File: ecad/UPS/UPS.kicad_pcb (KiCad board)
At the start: 4 copper layers, 121.9 x 139.7 mm, 163 parts, among them J2 Conn_01x02_Pin, J3 USB_C_Receptacle_USB2.0_16P, J4 PROG, J5 Conn_01x02_Pin, J6 Conn_01x02_Pin, J7 Fan_Connector, J8 PJ-002AH, Q1 CSD18540Q5B, Q2 Q_PMOS_DGS, Q3 IRLR7843TRPBF, Q4 Q_PMOS_DGS, Q5 CSD18540Q5B, Q6 CSD18540Q5B, Q7 CSD18540Q5B, Q8 2N7002, SW3 SW_DPDT_x2, U1 BQ25730RSNR, U2 MPQ5031GRE-0001-AEC1-P, U4 STM32L152RCT6, U5 AP2112K-3.3TRG1, U6 BOOT0, U7 NRST

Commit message: MCU routing
Routed most of MCU
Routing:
- net /Charger/bat_th1: track 0.00 -> 234.9 mm, vias 0 -> 4
- net /Charger/cmp_out: track 0.00 -> 216.1 mm, vias 0 -> 6
- net /Charger/PROCHOT_N: track 0.00 -> 146.7 mm, vias 0 -> 4
- net +3.3V: track 0.00 -> 136.6 mm, vias 0 -> 2
- net GND: track 27.8 -> 151.2 mm, vias 19 -> 21
- net /Charger/bat_th3: track 0.00 -> 120.5 mm, vias 0 -> 5
- net /Charger/bat_th2: track 0.00 -> 119.4 mm, vias 0 -> 4
- net /Output/vsel2: track 0.00 -> 89.6 mm, vias 0 -> 4
- net /controller/PB0: track 0.00 -> 82.5 mm, vias 0 -> 2
- net 3.3V: track 0.00 -> 80.3 mm, vias 0 -> 4
- net /Output/SDA: track 0.00 -> 80.1 mm, vias 0 -> 2
- net Net-(U4B-BOOT0): track 0.00 -> 76.6 mm, vias 0 -> 2
- net /Output/vsel1: track 0.00 -> 71.1 mm, vias 0 -> 2
- net /Output/SCL: track 0.00 -> 70.8 mm
- net NRST: track 0.00 -> 56.5 mm, vias 0 -> 4
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
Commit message: late night grind
Add battery and board thermistor circuits on PC0/PC1.

Implement ADC sampling, temperature conversion, and sensor fault reporting.

Enable the STM32 ADC drivers and poll temperatures in the main loop.

Add the OLED connector on PB10/PB11 and update PCB footprints and net assignments.

Add a Raspberry Pi mounting-hole footprint.

Exclude local docs and test folders from Git.
- checked routing
- messed with firmware
- planning final touches
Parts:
- added ?: , , F.Cu at (154.5, 159.5)
- added C71: 100nF, Capacitor_SMD:C_0805_2012Metric, F.Cu at (29.4, 135.5)
- added C72: 100nF, Capacitor_SMD:C_0805_2012Metric, F.Cu at (29.4, 138.5)
- added J10: NTC_10K_B3950, Connector_PinHeader_2.54mm:PinHeader_1x04_P2.54mm_Vertical, F.Cu at (19.0, 149.7)
- added J9: OLED_3V3_I2C2, Connector_PinHeader_2.54mm:PinHeader_1x04_P2.54mm_Vertical, F.Cu at (10.0, 136.2)
- added R45: 10k 1%, Resistor_SMD:R_0805_2012Metric, F.Cu at (29.4, 141.5)
- added R46: 10k 1%, Resistor_SMD:R_0805_2012Metric, F.Cu at (29.4, 144.4)
- added REF**: pi5_MountingHole_2.2mm_M2_Pad_58mm*49mm, UPS:MountingHole_2.2mm_M2_Pad_58mm_49mm_pi5, F.Cu at (197.5, 161.5)
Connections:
- U4 pad 29: unconnected-(U4B-PB10-Pad29) -> /controller/OLED_SCL
- U4 pad 30: unconnected-(U4B-PB11-Pad30) -> /controller/OLED_SDA
- U4 pad 8: unconnected-(U4B-PC0-Pad8) -> /controller/TEMP_BAT
- U4 pad 9: unconnected-(U4B-PC1-Pad9) -> /controller/TEMP_BOARD

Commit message: Organize UPS placement for Pi 5 mounting and power-stage review
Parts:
- removed ?: , 
- removed C65: 1nF, Capacitor_SMD:C_0603_1608Metric_Pad1.08x0.95mm_HandSolder
- removed C71: 100nF, Capacitor_SMD:C_0805_2012Metric
- removed R42: 4.7k, Resistor_SMD:R_0805_2012Metric
- removed R45: 10k 1%, Resistor_SMD:R_0805_2012Metric
- removed REF**: pi5_MountingHole_2.2mm_M2_Pad_58mm*49mm, UPS:MountingHole_2.2mm_M2_Pad_58mm_49mm_pi5
- added C73: 100 nF, Capacitor_SMD:C_0603_1608Metric, F.Cu at (107.0, 125.0)
- added H1: Pi5_M2.5_NPTH, MountingHole:MountingHole_2.7mm_M2.5, F.Cu at (83.5, 103.0)
- added H2: Pi5_M2.5_NPTH, MountingHole:MountingHole_2.7mm_M2.5, F.Cu at (141.5, 103.0)
- added H3: Pi5_M2.5_NPTH, MountingHole:MountingHole_2.7mm_M2.5, F.Cu at (83.5, 152.0)
- added H4: Pi5_M2.5_NPTH, MountingHole:MountingHole_2.7mm_M2.5, F.Cu at (141.5, 152.0)
- added J11: BAT3_10K_NTC, Connector_JST:JST_XH_B2B-XH-A_1x02_P2.50mm_Vertical, F.Cu at (54.3, 113.0)
- added J12: PI_UART, Connector_PinHeader_2.54mm:PinHeader_1x03_P2.54mm_Vertical, F.Cu at (53.0, 166.0)
- added R47: 10k 1%, Resistor_SMD:R_0805_2012Metric_Pad1.20x1.40mm_HandSolder, F.Cu at (103.5, 125.0)
- C39, C40, C41, C42, C43, C44: footprint Capacitor_SMD:C_0603_1608Metric -> Capacitor_SMD:C_1210_3225Metric
- C51, C52, C53, C54, C55, C56, C57: footprint Capacitor_SMD:C_0603_1608Metric -> Capacitor_SMD:C_0805_2012Metric
- J10: value NTC_10K_B3950 -> BOARD_10K_NTC
- J2: value Conn_01x02_Pin -> BAT1_10K_NTC
- J5: value Conn_01x02_Pin -> BAT2_10K_NTC
- J6: value Conn_01x02_Pin -> BAT4_10K_NTC
- R24, R28, R34: value 68.1k -> 10k 1%
- U1: footprint UPS:RSN0032B-IPC_C -> Package_DFN_QFN:Texas_RSN_WQFN-32-1EP_4x4mm_P0.4mm_EP2.8x2.8mm
- moved J2 95.4 mm to (54.3, 90.0), turned to 90 degrees
- moved U2 93.5 mm to (145.0, 48.0)
- moved COUT1 88.4 mm to (98.0, 121.0), turned to 90 degrees
- moved L2 86.1 mm to (154.0, 71.5), turned to -90 degrees
- moved R40 83.5 mm to (139.0, 41.0)
- moved J6 83.5 mm to (54.3, 74.5), turned to 90 degrees
- moved SW3 80.8 mm to (89.0, 85.0)
- moved CIN1 73.1 mm to (90.0, 121.0), turned to 90 degrees
- moved C20 72.5 mm to (152.0, 84.5)
- moved C64 70.5 mm to (140.5, 56.0)
- moved C9 69.6 mm to (141.0, 46.0), turned to 90 degrees
- moved J5 68.7 mm to (54.3, 102.0), turned to 90 degrees
- moved PS1 67.4 mm to (154.0, 87.5), turned to 0 degrees
- moved R7 67.2 mm to (149.5, 41.0), turned to 90 degrees
- moved J3 67.0 mm to (167.5, 47.5)
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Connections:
- net /Charger/bat_th3 renamed /Charger/bat_th4
- J10 pad 2: /controller/TEMP_BAT -> unconnected-(J10-Pin_2-Pad2)
- U4 pad 20: Net-(U4B-PA4) -> unconnected-(U4B-PA4-Pad20)
- U4 pad 58: unconnected-(U4B-PB6-Pad58) -> /controller/PI_UART_TX
- U4 pad 59: unconnected-(U4B-PB7-Pad59) -> /controller/PI_UART_RX
- U4 pad 8: /controller/TEMP_BAT -> bat_th3
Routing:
- net /Charger/bat_th1: track 234.9 -> 2.43 mm, vias 4 -> 1
- net /Charger/cmp_out: track 216.1 -> 13.3 mm, vias 6 -> 2
- net /Charger/PROCHOT_N: track 146.7 -> 22.8 mm, vias 4 -> 2
- net /Charger/bat_th4: track 120.5 -> 0.00 mm, vias 5 -> 0
- net /Charger/bat_th2: track 119.4 -> 20.9 mm, vias 4 -> 1
- net GND: track 151.2 -> 61.1 mm, vias 21 -> 8
- net /Output/SDA: track 80.1 -> 12.7 mm
- net /controller/PB0: track 82.5 -> 16.9 mm
- net Net-(U4B-BOOT0): track 76.6 -> 13.4 mm, vias 2 -> 0
- net /Output/SCL: track 70.8 -> 12.8 mm
- net Net-(U2-VDD): track 53.8 -> 0.00 mm
- net /Output/vsel1: track 71.1 -> 23.5 mm, vias 2 -> 1
- net Net-(D8-A): track 49.0 -> 3.44 mm
- net 3.3V: track 80.3 -> 37.2 mm, vias 4 -> 2
- net Net-(U1-LODRV1): track 34.0 -> 0.00 mm
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- added copper zone on B.Cu, net GND
- added copper zone on F.Cu, net GND
- removed copper zone on F.Cu, net /Charger/Charger_VBUS_IN
- removed copper zone on F.Cu, net Net-(U1-SW2)
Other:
- board text added: "5V POUR"
- board text added: "BATTERY + BUS CORRIDOR / SIZE FROM TEAM CALCS"
- board text added: "INPUT -> CHARGER -> VSYS -> BOOST -> OUTPUT"
- board text added: "PI 5 ENVELOPE / UPS BELOW / CHECK STANDOFF HEIGHT"
- board text added: "PLACEMENT CANDIDATE - NOT ROUTED / NOT FOR FAB"
- board text added: "QUIET CONTROL / KEEP SWITCH RETURNS LOCAL"
- board text added: "VBUS POUR"
- board text added: "VSYS POUR"

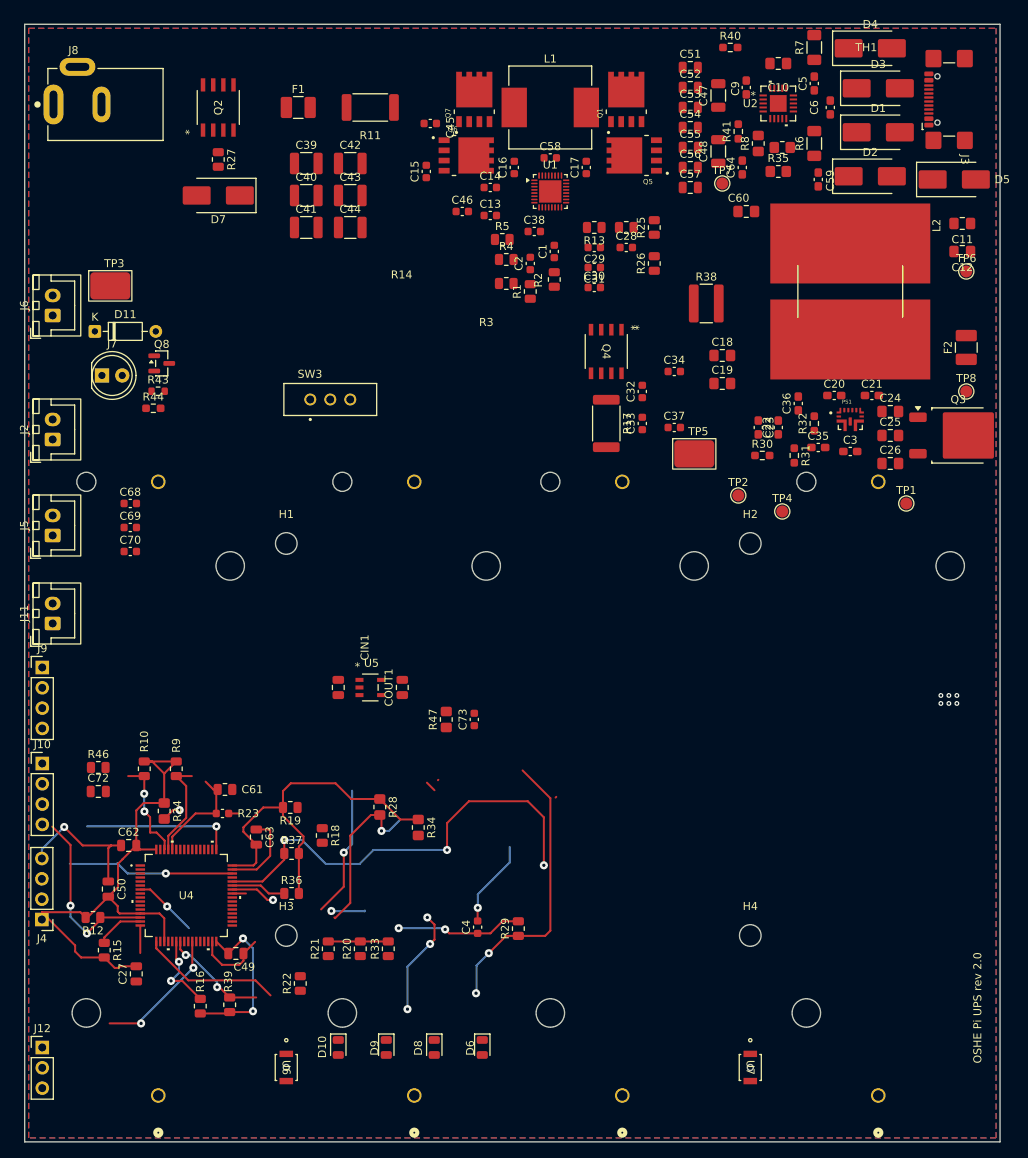
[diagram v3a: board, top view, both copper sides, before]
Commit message: Trial-route boost stage and define local power copper
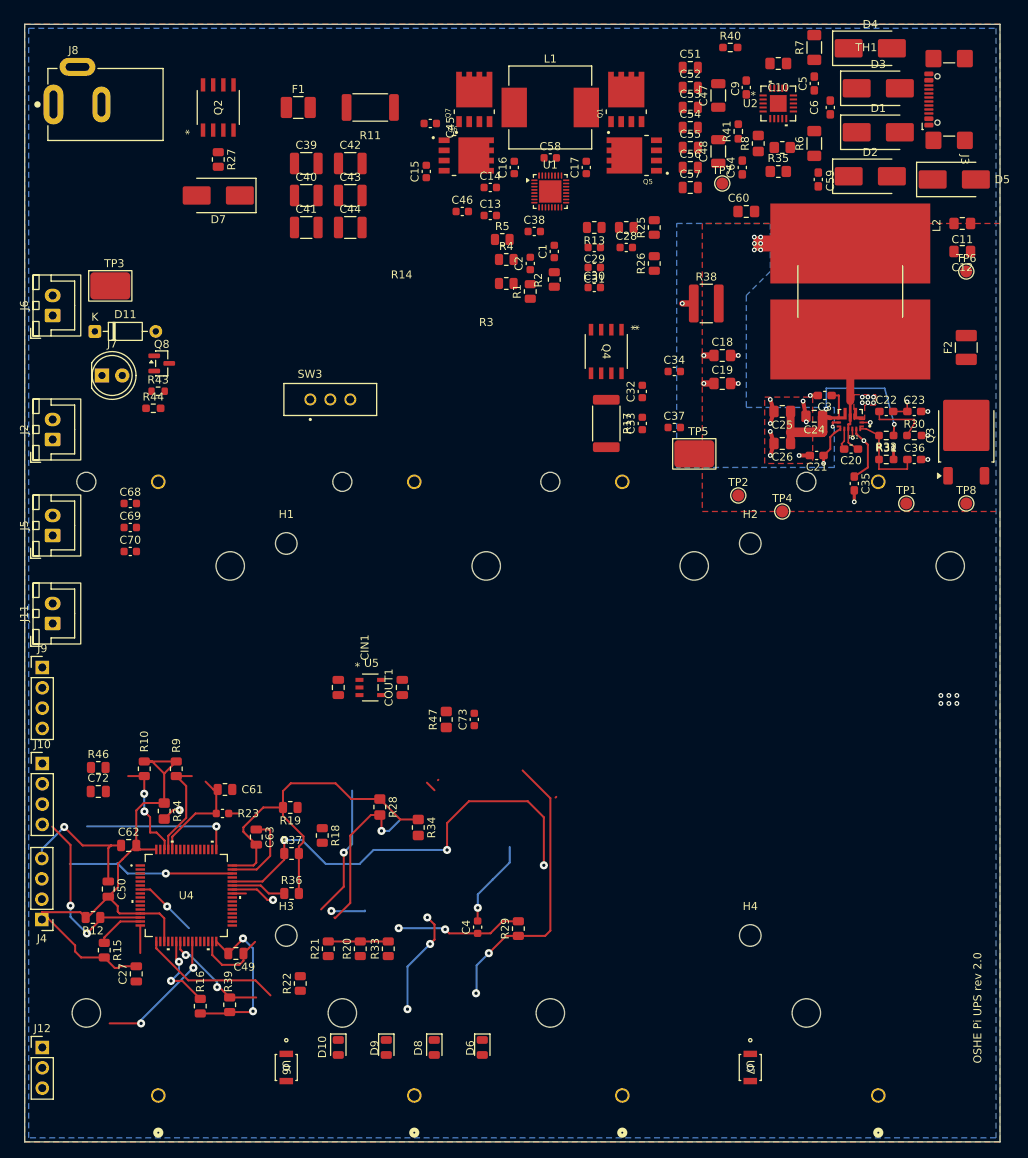
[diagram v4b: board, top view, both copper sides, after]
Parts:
- moved C23 19.6 mm to (162.0, 86.5), turned to 0 degrees
- moved R30 19.2 mm to (162.0, 89.5)
- moved C36 16.1 mm to (162.0, 92.5), turned to 0 degrees
- moved TP8 14.0 mm to (168.5, 98.0)
- moved C25 13.8 mm to (145.5, 86.5), turned to 180 degrees
- moved C26 13.7 mm to (145.5, 90.5), turned to 180 degrees
- moved C22 13.6 mm to (158.5, 86.5), turned to 0 degrees
- moved R31 11.5 mm to (158.5, 92.5), turned to 0 degrees
- moved C21 10.2 mm to (149.8, 92.0), turned to 180 degrees
- moved C24 9.52 mm to (149.5, 87.1), turned to 180 degrees
- moved R32 9.12 mm to (158.5, 89.5), turned to 180 degrees
- moved C3 7.70 mm to (150.8, 84.5), turned to 180 degrees
- moved C20 7.02 mm to (154.1, 91.2), turned to 180 degrees
- moved C35 6.36 mm to (154.5, 95.5), turned to -90 degrees
- moved Q3 1.00 mm to (168.5, 89.5), turned to 90 degrees
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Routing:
- net /BoostConvertor/vbus: track 0.00 -> 32.7 mm, vias 0 -> 2
- net GND: track 61.1 -> 80.7 mm, vias 8 -> 30
- net /BoostConvertor/Vcc: track 0.00 -> 15.4 mm, vias 0 -> 2
- net Net-(PS1-FB): track 0.00 -> 11.5 mm
- net Net-(PS1-VIN): track 0.00 -> 11.5 mm, vias 0 -> 10
- net Net-(C20-Pad1): track 0.00 -> 10.1 mm
- net Net-(PS1-COMP): track 0.00 -> 9.58 mm, vias 0 -> 2
- net Net-(C22-Pad1): track 0.00 -> 7.62 mm
- net Net-(PS1-BST): track 0.00 -> 2.75 mm
- added copper zone on B.Cu, net Net-(PS1-VIN)

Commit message: meow
basicaly nothing
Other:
- board text removed: "PI 5 ENVELOPE / UPS BELOW / CHECK STANDOFF HEIGHT"
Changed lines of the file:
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@@
+	)
+	(gr_line
+		(start 150 99)
+		(end 145.5 99)
+		(stroke
+			(width 0.2)
+			(type default)
+		)
+		(layer "F.Cu")
+		(net "/BoostConvertor/Vcc")
+	)
+	(gr_line
+		(start 154.5 94.5)
+		(end 150 99)
+		(stroke
+			(width 0.2)
+			(type default)
+		)
+		(layer "F.Cu")
+		(net "/BoostConvertor/Vcc")
 	)
 	(gr_line
@@
 	(gr_text "PLACEMENT CANDIDATE - NOT ROUTED / NOT FOR FAB"
 		(at 111 175.5 0)
-		(layer "Dwgs.User")
-		(effects
-			(font
-				(size 0.85 0.85)
-				(thickness 0.15)
-			)
-		)
-	)
-	(gr_text "PI 5 ENVELOPE / UPS BELOW / CHECK STANDOFF HEIGHT"
-		(at 118 114 0)
 		(layer "Dwgs.User")
 		(effects
@@
 			)
 		)
-	)
-	(zone
-		(net "GND")
-		(layer "F.Cu")
-		(name "GND_F.Cu")
-		(hatch edge 0.5)
-		(connect_pads
-			(clearance 0.25)
-		)
-		(min_thickness 0.2)
-		(fill yes
-			(thermal_gap 0.25)
-			(thermal_bridge_width 0.4)
-			(island_removal_mode 0)
-		)
-		(polygon
-			(pts
-				(xy 50.8 38.1) (xy 172.72 38.1) (xy 172.72 63) (xy 135.5 63) (xy 135.5 99) (xy 172.72 99) (xy 172.72 177.8)
-				(xy 50.8 177.8)
-			)
-		)

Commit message: bazinga
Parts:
- J11, J2, J5, J6: moved to B.Cu
- moved J5 92.9 mm to (141.5, 134.0)
- moved J2 92.2 mm to (141.5, 120.0)
- moved C68 80.2 mm to (131.0, 142.0)
- moved C69 73.5 mm to (125.0, 142.0)
- moved C70 66.9 mm to (119.0, 142.0)
- moved J6 66.3 mm to (83.5, 134.0)
- moved R24 50.8 mm to (119.0, 139.0), turned to 0 degrees
- moved U6 48.5 mm to (132.0, 167.0)
- moved C62 34.5 mm to (97.5, 133.5), turned to 180 degrees
- moved C27 33.8 mm to (98.0, 150.5), turned to 0 degrees
- moved C50 31.2 mm to (92.4, 144.0), turned to 0 degrees
- moved R34 31.0 mm to (131.0, 139.0), turned to 0 degrees
- moved J11 30.9 mm to (83.5, 123.0)
- moved R12 30.8 mm to (90.0, 146.5)
- moved R36 30.8 mm to (110.0, 130.0)
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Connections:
- C61 pad 2: 3.3V -> +3.3V
- Q7 pad 4: GND -> Net-(U1-HIDRV1)
- R29 pad 1: 3.3V -> +3.3V
- U1 pad 31: GND -> Net-(U1-HIDRV1)
- U6 pad 2: 3.3V -> +3.3V
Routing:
- net +5V: track 0.00 -> 242.8 mm, vias 0 -> 11
- net /Output/SCL: track 12.8 -> 152.9 mm, vias 0 -> 12
- net /Output/SDA: track 12.7 -> 151.5 mm, vias 2 -> 11
- net /Charger/chrg_ok: track 6.00 -> 131.5 mm, vias 0 -> 4
- net /Charger/OTG/VAP: track 10.1 -> 130.6 mm, vias 2 -> 3
- net /Charger/VBAT_SENSE: track 0.00 -> 118.1 mm, vias 0 -> 13
- net +3.3V: track 136.6 -> 251.3 mm, vias 2 -> 33
- net /Charger/CMPIN: track 0.00 -> 110.2 mm, vias 0 -> 6
- net /Charger/cmp_out: track 13.3 -> 121.4 mm, vias 2 -> 5
- net /Output/vsel1: track 23.5 -> 122.2 mm, vias 1 -> 8
- net /Charger/PROCHOT_N: track 22.8 -> 113.1 mm, vias 2 -> 6
- net Net-(Q3-G): track 0.00 -> 83.6 mm, vias 0 -> 2
- net Net-(SW3A-A): track 0.00 -> 76.7 mm, vias 0 -> 2
- net /controller/PB0: track 16.9 -> 83.9 mm, vias 2 -> 9
- net /controller/OLED_SDA: track 0.00 -> 65.6 mm, vias 0 -> 4
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- added copper zone on B.Cu, net +5V
- added copper zone on F.Cu, net +5V
- added copper zone on B.Cu, net /BoostConvertor/vbus
- added copper zone on F.Cu, net /BoostConvertor/vbus
- added copper zone on F.Cu, net /Charger/Charger_VBUS_IN
- added copper zone on B.Cu, net /Charger/VBAT_SENSE
- added copper zone on F.Cu, net /Charger/VBAT_SENSE
- added copper zone on B.Cu, net /Output/VBUS_out
- added copper zone on F.Cu, net /Output/VBUS_out
- added copper zone on B.Cu, net Net-(J8-Pad1)
- added copper zone on F.Cu, net Net-(J8-Pad1)
- added copper zone on F.Cu, net Net-(U1-ACN)
- added copper zone on F.Cu, net Net-(U1-SRP)
- added copper zone on F.Cu, net Net-(U1-SW2)
- added copper zone on F.Cu, net PMOS_IN_GATE
- added copper zone on B.Cu, net PMOS_OUT_GATE
- added copper zone on F.Cu, net PMOS_OUT_GATE
- added copper zone on F.Cu, net SW1
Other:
- board text added: "BOARD NTC"
- board text added: "BOOT"
- board text added: "GPIO BUTTON SPACE"
- board text added: "NTC1"
- board text added: "NTC2"
- board text added: "NTC3"
- board text added: "NTC4"
- board text added: "OLED"
- board text added: "PI UART"
- board text added: "RESET"
- board text added: "SWD"
